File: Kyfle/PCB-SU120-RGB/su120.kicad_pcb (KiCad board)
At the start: 2 copper layers, 98 x 98 mm, 427 parts, among them J1 MJ-4PP-9, J2 Conn_01x03, J3 Conn_01x08, J4 Conn_01x08, J6 MJ-4PP-9, J7 Conn_02x05_Odd_Even, J8 Conn_02x05_Odd_Even, SW1 SW_PUSH_LED, SW10 SW_PUSH_LED, SW11 SW_PUSH_LED, SW12 SW_PUSH_LED, SW13 SW_PUSH_LED, SW14 SW_PUSH_LED, SW15 SW_PUSH_LED, SW16 SW_PUSH_LED, SW17 SW_PUSH_LED, SW18 SW_PUSH_LED, SW2 SW_PUSH_LED, SW20 Rotary_Encoder_Switch, SW21 Rotary_Encoder_Switch, SW22 SW_Push, SW3 SW_PUSH_LED, SW4 SW_PUSH_LED, SW5 SW_PUSH_LED, SW6 SW_PUSH_LED, SW7 SW_PUSH_LED, SW8 SW_PUSH_LED, SW9 SW_PUSH_LED, U1 ProMicro

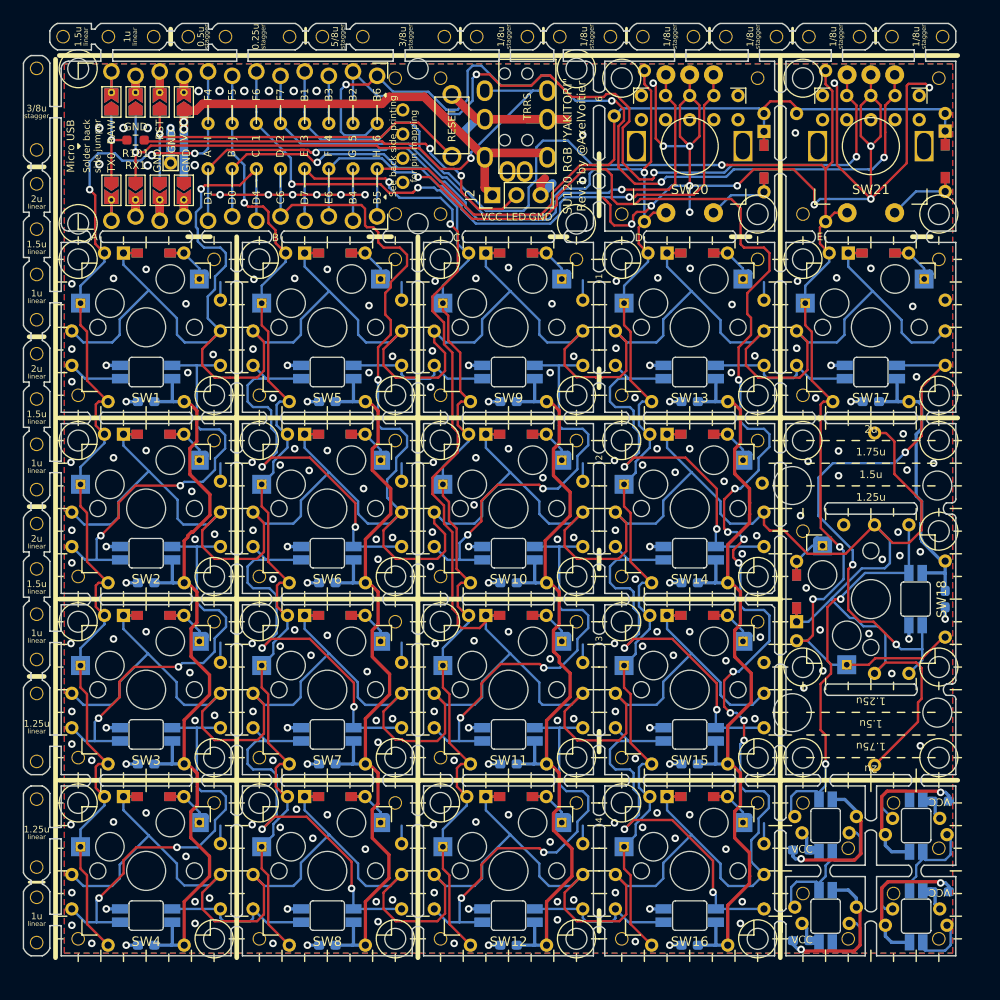
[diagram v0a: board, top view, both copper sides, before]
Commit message: Massive reduction in drill impacts and drill size diversity
It was suggested by a redittor that jlcpcb might charge engineering fees for too many holes.
So, all biscuits have been removed, all unused M1.4 holes have been removed, the signal pads (column, row, din, dout) have been converted from holes to just SMD pads as it should be fine if using enameled wire.
And the various holes have been harmonised to minimise number of drill sizes.

Also, number of vias have been greatly reduced, at the price of a bit less copper pour here and there (that's ok, if we cared about signal integrity we would you at least use a 4 layer stack up...).
The slots have been redone as footprints in order to control more easily their profile and achieve a consistent 1.2mm wide slot (including correct termination radius).

Finally, the Pro micro footprint has been switched to non-zigzag and rather use (tentative) a rivet-based socketing design.

All that came at the price of pretty much re-routing the entire board, again...
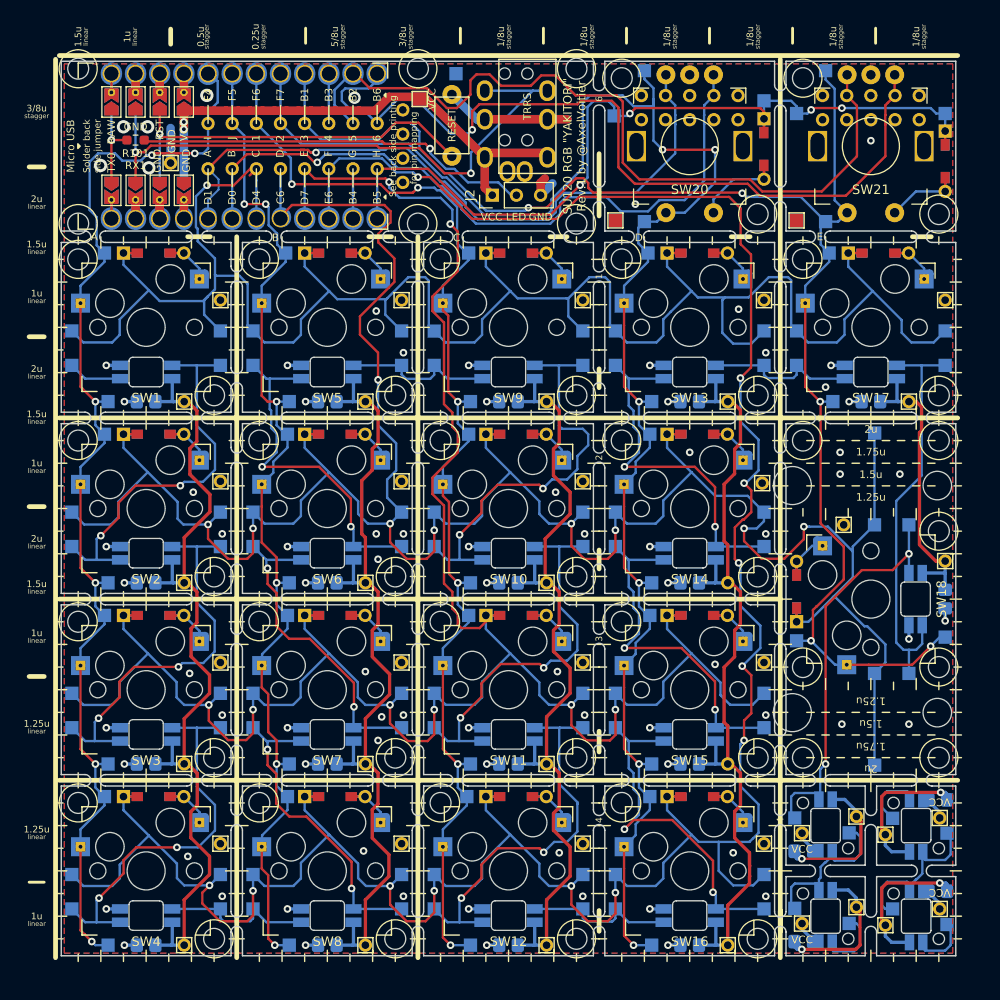
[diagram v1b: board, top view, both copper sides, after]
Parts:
- removed the ? at (82.5, 59.5)
- removed the ? at (82.5, 73.8)
- removed the ? at (77.8, 73.8)
- removed the ? at (42.9, 55.2)
- removed the ? at (52.4, 55.2)
- removed the ? at (47.6, 55.2)
- removed the ? at (40.1, 145.7)
- removed the ? at (40.1, 150.4)
- removed the ? at (40.1, 80.2)
- removed the ? at (40.1, 75.4)
- removed the ? at (40.1, 84.9)
- removed the ? at (40.1, 70.6)
- removed the ? at (40.1, 88.5)
- removed the ? at (40.1, 98.0)
- removed the ? at (40.1, 102.8)
- removed the ? at (40.1, 93.3)
- removed the ? at (56.0, 55.2)
- removed the ? at (59.9, 55.2)
- removed the ? at (66.7, 55.2)
- removed the ? at (40.1, 106.4)
- removed the ? at (40.1, 111.1)
- removed the ? at (40.1, 120.7)
- removed the ? at (40.1, 115.9)
- removed the ? at (40.1, 131.4)
- removed the ? at (40.1, 124.2)
- removed the ? at (40.1, 142.5)
- removed the ? at (40.1, 135.3)
- removed the ? at (70.1, 55.2)
- removed the ? at (82.9, 55.2)
- removed the ? at (74.4, 55.2)
- removed the ? at (40.1, 58.5)
- removed the ? at (40.1, 67.1)
- removed the ? at (115.9, 59.5)
- removed the ? at (134.9, 59.5)
- removed the ? at (120.7, 73.8)
- removed the ? at (101.6, 73.8)
- removed the ? at (58.7, 78.6)
- removed the ? at (77.8, 78.6)
- removed the ? at (96.8, 78.6)
- removed the ? at (115.9, 78.6)
- removed the ? at (134.9, 78.6)
- removed the ? at (120.7, 92.9)
- removed the ? at (101.6, 92.9)
- removed the ? at (82.5, 92.9)
- removed the ? at (63.5, 92.9)
- removed the ? at (44.5, 92.9)
- removed the ? at (58.7, 97.6)
- removed the ? at (77.8, 97.6)
- removed the ? at (96.8, 97.6)
- removed the ? at (115.9, 97.6)
- removed the ? at (58.7, 135.7)
- removed the ? at (44.5, 150.0)
- removed the ? at (101.6, 111.9)
- removed the ? at (82.5, 111.9)
- removed the ? at (63.5, 111.9)
- removed the ? at (44.5, 111.9)
- removed the ? at (58.7, 116.7)
- removed the ? at (77.8, 116.7)
- removed the ? at (96.8, 116.7)
- removed the ? at (115.9, 116.7)
- removed the ? at (77.8, 135.7)
- removed the ? at (63.5, 150.0)
- removed the ? at (101.6, 131.0)
- removed the ? at (82.5, 131.0)
- removed the ? at (63.5, 131.0)
- removed the ? at (44.5, 131.0)
- removed the ? at (120.7, 107.2)
- removed the ? at (115.9, 135.7)
- removed the ? at (96.8, 135.7)
- removed the ? at (82.5, 150.0)
- removed the ? at (101.6, 150.0)
- removed the ? at (130.0, 55.2)
- removed the ? at (135.3, 55.2)
- removed the ? at (91.7, 55.2)
- removed the ? at (86.4, 55.2)
- removed the ? at (121.3, 55.2)
- removed the ? at (112.5, 55.2)
- removed the ? at (117.9, 55.2)
- removed the ? at (126.6, 55.2)
- removed the ? at (95.1, 55.2)
- removed the ? at (77.8, 59.5)
- removed the ? at (100.4, 55.2)
- removed the ? at (109.1, 55.2)
- removed the ? at (103.8, 55.2)
- added H168: MountingHole_Pad, #footprint:1pad_conn, F.Cu at (80.4, 61.7)
- added H169: MountingHole_Pad, #footprint:1pad_conn, B.Cu at (84.2, 59.1)
- added H170: MountingHole_Pad, #footprint:1pad_conn, F.Cu at (100.9, 74.5)
- added H171: MountingHole_Pad, #footprint:1pad_conn, F.Cu at (120.0, 74.5)
- added REF**: Slot_1.2mm_9.2mm, #footprint:Slot_Line_1.2mm_8.66mm, F.Cu at (118.3, 66.7)
- added REF**: Slot_1.2mm_7.4.mm, #footprint:Slot_Cross_1.2mm_7.4mm_6.85mm, F.Cu at (99.2, 95.2)
- added REF**: Slot_1.2mm_7.4.mm, #footprint:Slot_Cross_1.2mm_7.4mm_6.85mm, F.Cu at (61.1, 95.2)
- added REF**: Slot_1.2mm_7.4.mm, #footprint:Slot_Cross_1.2mm_7.4mm_6.85mm, F.Cu at (80.2, 95.2)
- added REF**: Slot_1.2mm_7.4.mm, #footprint:Slot_Cross_1.2mm_7.4mm_6.85mm, F.Cu at (80.2, 114.3)
- added REF**: Slot_1.2mm_7.4.mm, #footprint:Slot_Cross_1.2mm_7.4mm_6.85mm, F.Cu at (99.2, 114.3)
- added REF**: Slot_1.2mm_7.4.mm, #footprint:Slot_Cross_1.2mm_7.4mm_6.85mm, F.Cu at (99.2, 133.3)
- added REF**: Slot_1.2mm_7.4.mm, #footprint:Slot_Cross_1.2mm_7.4mm, F.Cu at (118.3, 76.2)
- added REF**: Slot_1.2mm_7.4.mm, #footprint:Slot_Cross_1.2mm_7.4mm, F.Cu at (118.3, 95.2)
- added REF**: Slot_1.2mm_7.4.mm, #footprint:Slot_Cross_1.2mm_7.4mm, F.Cu at (118.3, 133.3)
- added REF**: Slot_1.2mm_7.4.mm, #footprint:Slot_Cross_1.2mm_7.4mm, F.Cu at (80.2, 133.3)
- added REF**: Slot_1.2mm_9.2mm, #footprint:Slot_Line_1.2mm_8.66mm, F.Cu at (99.2, 66.7)
- added REF**: Slot_1.2mm_7.4.mm, #footprint:Slot_Cross_1.2mm_7.4mm, F.Cu at (61.1, 133.3)
- added REF**: Slot_1.2mm_7.4.mm, #footprint:Slot_Cross_1.2mm_7.4mm, F.Cu at (61.1, 114.3)
- added REF**: Slot_1.2mm_3.7.mm, #footprint:Slot_Line_1.2mm_3.7mm, F.Cu at (99.2, 57.2)
- added REF**: Slot_1.2mm_3.7.mm, #footprint:Slot_Line_1.2mm_3.7mm, F.Cu at (118.3, 57.2)
- added REF**: Slot_1.2mm_3.7.mm, #footprint:Slot_Line_1.2mm_3.7mm, F.Cu at (118.3, 152.4)
- added REF**: Slot_1.2mm_3.7.mm, #footprint:Slot_Line_1.2mm_3.7mm, F.Cu at (127.8, 152.4)
- added REF**: Slot_1.2mm_3.7.mm, #footprint:Slot_Line_1.2mm_3.7mm, F.Cu at (137.3, 142.9)
- added REF**: Slot_1.2mm_3.7.mm, #footprint:Slot_Line_1.2mm_3.7mm, F.Cu at (137.3, 133.3)
- added REF**: Slot_1.2mm_3.7.mm, #footprint:Slot_Line_1.2mm_3.7mm, F.Cu at (137.3, 76.2)
- added REF**: Slot_1.2mm_3.7.mm, #footprint:Slot_Line_1.2mm_3.7mm, F.Cu at (137.3, 95.2)
- added REF**: Slot_1.2mm_7.4.mm, #footprint:Slot_Cross_1.2mm_7.4mm, F.Cu at (99.2, 76.2)
- added REF**: Slot_1.2mm_3.7.mm, #footprint:Slot_Line_1.2mm_3.7mm, F.Cu at (99.2, 152.4)
- added REF**: Slot_1.2mm_3.7.mm, #footprint:Slot_Line_1.2mm_3.7mm, F.Cu at (80.2, 152.4)
- added REF**: Slot_1.2mm_3.7.mm, #footprint:Slot_Line_1.2mm_3.7mm, F.Cu at (61.1, 152.4)
- added REF**: Slot_1.2mm_3.7.mm, #footprint:Slot_Line_1.2mm_3.7mm, F.Cu at (42.1, 133.3)
- added REF**: Slot_1.2mm_3.7.mm, #footprint:Slot_Line_1.2mm_3.7mm, F.Cu at (42.1, 114.3)
- added REF**: Slot_1.2mm_3.7.mm, #footprint:Slot_Line_1.2mm_3.7mm, F.Cu at (42.1, 95.2)
- added REF**: Slot_1.2mm_3.7.mm, #footprint:Slot_Line_1.2mm_3.7mm, F.Cu at (42.1, 76.2)
- added REF**: Slot_1.2mm_9.75mm, #footprint:Slot_Line_1.2mm_9.75mm, F.Cu at (118.3, 104.8)
- added REF**: Slot_1.2mm_9.75mm, #footprint:Slot_Line_1.2mm_9.75mm, F.Cu at (118.3, 123.8)
- added REF**: Slot_1.2mm_9.75mm, #footprint:Slot_Line_1.2mm_9.75mm, F.Cu at (70.6, 76.2)
- added REF**: Slot_1.2mm_7.4.mm, #footprint:Slot_Tee_1.2mm_7.4mm, F.Cu at (118.3, 114.3)
- added REF**: Slot_1.2mm_9.75mm, #footprint:Slot_Line_1.2mm_9.75mm, F.Cu at (61.1, 142.9)
- added REF**: Slot_1.2mm_9.75mm, #footprint:Slot_Line_1.2mm_9.75mm, F.Cu at (80.2, 142.9)
- added REF**: Slot_1.2mm_9.75mm, #footprint:Slot_Line_1.2mm_9.75mm, F.Cu at (99.2, 142.9)
- added REF**: Slot_1.2mm_9.75mm, #footprint:Slot_Line_1.2mm_9.75mm, F.Cu at (99.2, 123.8)
- added REF**: Slot_1.2mm_9.75mm, #footprint:Slot_Line_1.2mm_9.75mm, F.Cu at (80.2, 123.8)
- added REF**: Slot_1.2mm_9.75mm, #footprint:Slot_Line_1.2mm_9.75mm, F.Cu at (61.1, 123.8)
- added REF**: Slot_1.2mm_9.75mm, #footprint:Slot_Line_1.2mm_9.75mm, F.Cu at (61.1, 104.8)
- added REF**: Slot_1.2mm_9.75mm, #footprint:Slot_Line_1.2mm_9.75mm, F.Cu at (80.2, 104.8)
- added REF**: Slot_1.2mm_9.75mm, #footprint:Slot_Line_1.2mm_9.75mm, F.Cu at (99.2, 104.8)
- added REF**: Slot_1.2mm_9.75mm, #footprint:Slot_Line_1.2mm_9.75mm, F.Cu at (118.3, 85.7)
- added REF**: Slot_1.2mm_7.4.mm, #footprint:Slot_Tee_1.2mm_7.4mm, F.Cu at (80.2, 76.2)
- added REF**: Slot_1.2mm_9.75mm, #footprint:Slot_Line_1.2mm_9.75mm, F.Cu at (99.2, 85.7)
- added REF**: Slot_1.2mm_9.75mm, #footprint:Slot_Line_1.2mm_9.75mm, F.Cu at (80.2, 85.7)
- added REF**: Slot_1.2mm_9.75mm, #footprint:Slot_Line_1.2mm_9.75mm, F.Cu at (61.1, 85.7)
- added REF**: Slot_1.2mm_9.75mm, #footprint:Slot_Line_1.2mm_9.75mm, F.Cu at (127.8, 95.2)
- added REF**: Slot_1.2mm_9.75mm, #footprint:Slot_Line_1.2mm_9.75mm, F.Cu at (127.8, 76.2)
- added REF**: Slot_1.2mm_9.75mm, #footprint:Slot_Line_1.2mm_9.75mm, F.Cu at (108.7, 76.2)
- added REF**: Slot_1.2mm_9.75mm, #footprint:Slot_Line_1.2mm_9.75mm, F.Cu at (108.7, 95.2)
- added REF**: Slot_1.2mm_9.75mm, #footprint:Slot_Line_1.2mm_9.75mm, F.Cu at (108.7, 114.3)
- added REF**: Slot_1.2mm_9.75mm, #footprint:Slot_Line_1.2mm_9.75mm, F.Cu at (108.7, 133.3)
- added REF**: Slot_1.2mm_9.75mm, #footprint:Slot_Line_1.2mm_9.75mm, F.Cu at (89.7, 133.3)
- added REF**: Slot_1.2mm_7.4.mm, #footprint:Slot_Tee_1.2mm_7.4mm, F.Cu at (61.1, 76.2)
- added REF**: Slot_1.2mm_9.75mm, #footprint:Slot_Line_1.2mm_9.75mm, F.Cu at (89.7, 114.3)
- added REF**: Slot_1.2mm_9.75mm, #footprint:Slot_Line_1.2mm_9.75mm, F.Cu at (89.7, 95.2)
- added REF**: Slot_1.2mm_9.75mm, #footprint:Slot_Line_1.2mm_9.75mm, F.Cu at (89.7, 76.2)
- added REF**: Slot_1.2mm_9.75mm, #footprint:Slot_Line_1.2mm_9.75mm, F.Cu at (70.6, 95.2)
- added REF**: Slot_1.2mm_9.75mm, #footprint:Slot_Line_1.2mm_9.75mm, F.Cu at (70.6, 114.3)
- added REF**: Slot_1.2mm_9.75mm, #footprint:Slot_Line_1.2mm_9.75mm, F.Cu at (70.6, 133.3)
- added REF**: Slot_1.2mm_9.75mm, #footprint:Slot_Line_1.2mm_9.75mm, F.Cu at (51.6, 133.3)
- added REF**: Slot_1.2mm_9.75mm, #footprint:Slot_Line_1.2mm_9.75mm, F.Cu at (51.6, 114.3)
- added REF**: Slot_1.2mm_9.75mm, #footprint:Slot_Line_1.2mm_9.75mm, F.Cu at (51.6, 95.2)
- added REF**: Slot_1.2mm_9.75mm, #footprint:Slot_Line_1.2mm_9.75mm, F.Cu at (51.6, 76.2)
- added REF**: Slot_1.2mm_9.75mm, #footprint:Slot_Tee_1.2mm_9.75mm, F.Cu at (118.3, 142.9)
- added REF**: Slot_1.2mm_9.75mm, #footprint:Slot_Tee_1.2mm_9.75mm, F.Cu at (127.8, 133.3)
- added REF**: Slot_1.2mm_9.75mm, #footprint:Slot_Cross_1.2mm_9.75mm, F.Cu at (127.8, 142.9)
- ?: footprint #footprint:CherryMX_Choc_Hotswap_2U_Outline -> #footprint:CherryMX_MidHeight_Choc_Hotswap_2U_Outline
- ? (x2): footprint #footprint:M2_Hole -> #footprint:M2_Hole_Standoff
- ? (x8): footprint #footprint:M1.4_tapping_Hole_rev2 -> #footprint:M1.4_tapping_Hole
- C1, C10, C11, C12, C13, C14, C15, C16, C17, C18, C19, C2, C20, C21, C22, C3, C4, C5, C6, C7, C8, C9: footprint Capacitor_SMD:C_0603_1608Metric_Pad1.08x0.95mm_HandSolder -> #footprint:C_0603_0805_HandSolder
- H1, H10, H100, H102, H104, H106, H108, H11, H110, H112, H113, H114, H115, H116, H117, H118, H119, H12, H120, H121, H122, H123, H124, H125, H126, H127, H128, H129, H13, H130, H131, H132, H133, H134, H135, H136, H137, H138, H139, H14, H140, H142, H145, H147, H149, H15, H151, H153, H154, H157, H158, H16, H161, H162, H165, H166, H17, H18, H19, H2, H20, H21, H210, H211, H212, H213, H22, H23, H24, H25, H26, H27, H28, H29, H3, H30, H31, H32, H33, H34, H35, H36, H37, H38, H39, H4, H40, H41, H42, H43, H44, H45, H46, H47, H48, H49, H5, H50, H51, H53, H55, H59, H6, H61, H63, H65, H67, H69, H7, H71, H72, H74, H76, H78, H8, H80, H82, H84, H87, H89, H9, H91, H93, H95, H97, H99: footprint #footprint:1pin_conn -> #footprint:1pad_conn; moved to B.Cu
- H101, H107, H109, H111, H141, H143, H144, H146, H148, H150, H152, H155, H156, H159, H160, H163, H164, H167, H52, H54, H56, H58, H60, H62, H64, H66, H68, H70, H73, H75, H77, H79, H81, H83, H85, H86, H88, H90, H92, H94, H96, H98: moved to B.Cu
- J2: footprint Connector_PinHeader_2.54mm:PinHeader_1x03_P2.54mm_Vertical -> #footprint:PinHeader_1x03_P2.54mm_Vertical
- U1: footprint #footprint:ArduinoProMicro-ZigZag_rev5 -> #footprint:ArduinoProMicro-Rivets
- moved D18 1.33 mm to (116.6, 64.2)
- moved H138 1.33 mm to (116.6, 61.9)
- moved C22 0.32 mm to (134.8, 135.4)
- moved C19 0.31 mm to (120.7, 140.8)
- moved C21 0.30 mm to (134.8, 145.0)
- moved C20 0.29 mm to (120.7, 150.3)
- moved H154 0.15 mm to (119.8, 137.3)
- moved H166 0.15 mm to (135.8, 138.9)
- moved H158 0.13 mm to (119.8, 146.8)
- moved H162 0.08 mm to (135.8, 148.5)
- turned H41 to 270 degrees
- turned H43 to 270 degrees
- turned H45 to 270 degrees
- turned H46 to 270 degrees
- turned H49 to 270 degrees
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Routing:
- net GND: track 302.9 -> 143.0 mm, vias 246 -> 85
- net Y2: track 312.9 -> 279.5 mm, vias 1 -> 9
- net Y4: track 321.6 -> 291.3 mm, vias 10 -> 12
- net Y1: track 251.9 -> 225.2 mm
- net X4: track 172.2 -> 189.0 mm, vias 1 -> 6
- net Y3: track 248.9 -> 234.9 mm, vias 2 -> 8
- net Net-(H145-Pad1): track 57.0 -> 43.0 mm, vias 3 -> 0
- net Net-(H149-Pad1): track 41.4 -> 33.2 mm
- net X5: track 169.2 -> 161.3 mm, vias 3 -> 5
- net Net-(H67-Pad1): track 41.1 -> 33.5 mm
- net X8: track 92.9 -> 88.1 mm, vias 4 -> 1
- net Net-(H65-Pad1): track 41.2 -> 36.8 mm
- net VCC: track 451.2 -> 446.9 mm
- net Net-(H104-Pad1): track 41.1 -> 36.9 mm
- net Net-(H102-Pad1): track 41.8 -> 37.7 mm
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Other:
- board size 98 x 98 mm -> 94 x 94 mm
- rule pad_to_mask_clearance: 0.2 -> 0.05

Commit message: Redid some footprints
- For the pro-micro socketed with rivets, it is now reversible
- The connector for OLED screen has also been converted to a rivetted version
- The footprint of the TRRS connector has been corrected according to part datasheet
- The silkscreen indicating the cut line in between bit boards is now done in some slots footprints
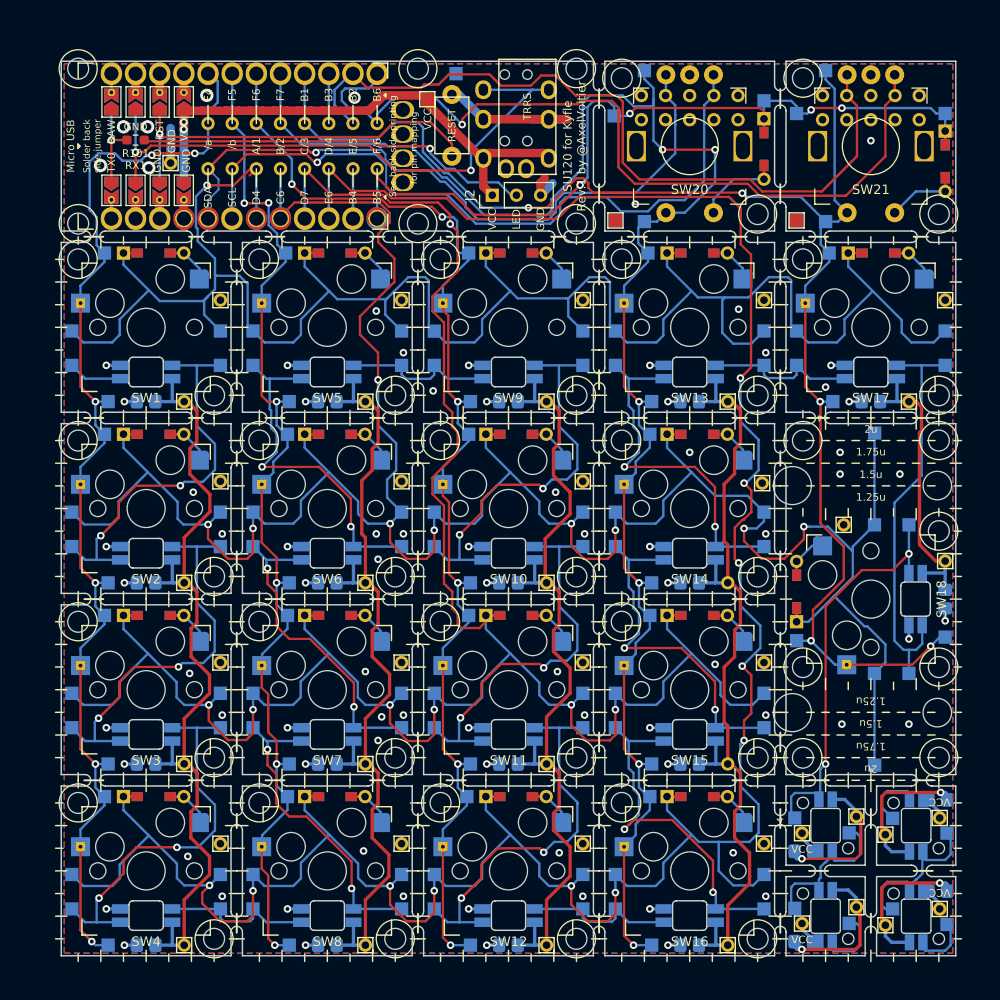
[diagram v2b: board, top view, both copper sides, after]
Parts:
- ?: footprint #footprint:OLED -> #footprint:OLED_rivet
- moved H168 0.79 mm to (81.2, 61.7)
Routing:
- net X7: track 84.5 -> 81.7 mm
- net Net-(H82-Pad1): track 43.6 -> 41.4 mm
- net GND: track 143.0 -> 141.5 mm, vias 85 -> 86
- net Y4: track 291.3 -> 289.9 mm, vias 12 -> 11
- net X8: track 88.1 -> 86.9 mm
- net X10: track 74.8 -> 75.9 mm
- net Y3: track 234.9 -> 233.9 mm, vias 8 -> 7
- net data: track 63.1 -> 62.1 mm
- net X3: track 133.6 -> 132.7 mm
- net reset1: track 40.4 -> 41.2 mm
- net Y6: track 89.5 -> 90.0 mm
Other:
- net class Default: clearance 0.2 -> 0.1524
- rule trace_clearance: 0.2 -> 0.1524
- board text added: "/a"
- board text added: "/b"
- board text added: "A/1"
- board text added: "B/2"
- board text added: "C/3"
- board text added: "D/4"
- board text added: "E/5"
- board text added: "F/6"
- board text added: "SCL"
- board text added: "SDA"
- board text added: "SU120 for Kyfle Rev.1 by @AxelVoitier"
- board text removed: "0.25u"
- board text removed: "0.5u"
- board text removed: "1"
- board text removed: "1.25u"
- board text removed: "1.5u"
- board text removed: "1/8u"
- board text removed: "1u"
- board text removed: "2"
- board text removed: "2u"
- board text removed: "3"
- board text removed: "3/8u"
- board text removed: "5"
- board text removed: "5/8u"
- board text removed: "6"
- board text removed: "C"
- board text removed: "D"
- board text removed: "D0"
- board text removed: "D1"
- board text removed: "E"
- board text removed: "F"
- board text removed: "G"
- board text removed: "H"
- board text removed: "I"
- board text removed: "J"
- board text removed: "SU120 RGB "YAKITORI" Rev.1 by @AxelVoitier"
- board text removed: "linear"
- board text removed: "stagger"
